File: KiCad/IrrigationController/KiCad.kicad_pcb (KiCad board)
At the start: 2 copper layers, 121.5 x 115 mm, 118 parts, among them IC1 MCP23017-E_SO, IC2 MCP23017-E_SO, IC3 DS89C21TMX_NOPB, J1 Screw_Terminal_01x03, J10 Screw_Terminal_01x05, J11 Screw_Terminal_01x02, J12 Screw_Terminal_01x02, J13 Screw_Terminal_01x04, J14 Screw_Terminal_01x02, J15 Screw_Terminal_01x02, J16 Screw_Terminal_01x02, J17 Screw_Terminal_01x02, J18 Screw_Terminal_01x02, J19 Screw_Terminal_01x02, J2 Screw_Terminal_01x03, J21 Screw_Terminal_01x06, J3 Screw_Terminal_01x03, J5 Screw_Terminal_01x03, J6 Screw_Terminal_01x02, J7 Screw_Terminal_01x02, J8 Screw_Terminal_01x02, J9 Screw_Terminal_01x02, K1 2071556-9, K2 2071556-9, Q1 MMBT3906, Q11 MMBT3904, Q12 MMBT3904, Q2 MMBT3906, Q3 MMBT3906, Q6 MMBT3904, Q7 MMBT3904, Q8 MMBT3904, SW1 SW_Push, U1 L298P, U2 ARDUINO_MKR_WAN_1310, U3 L298P, U4 L298P, U5 L298P, U7 L7805

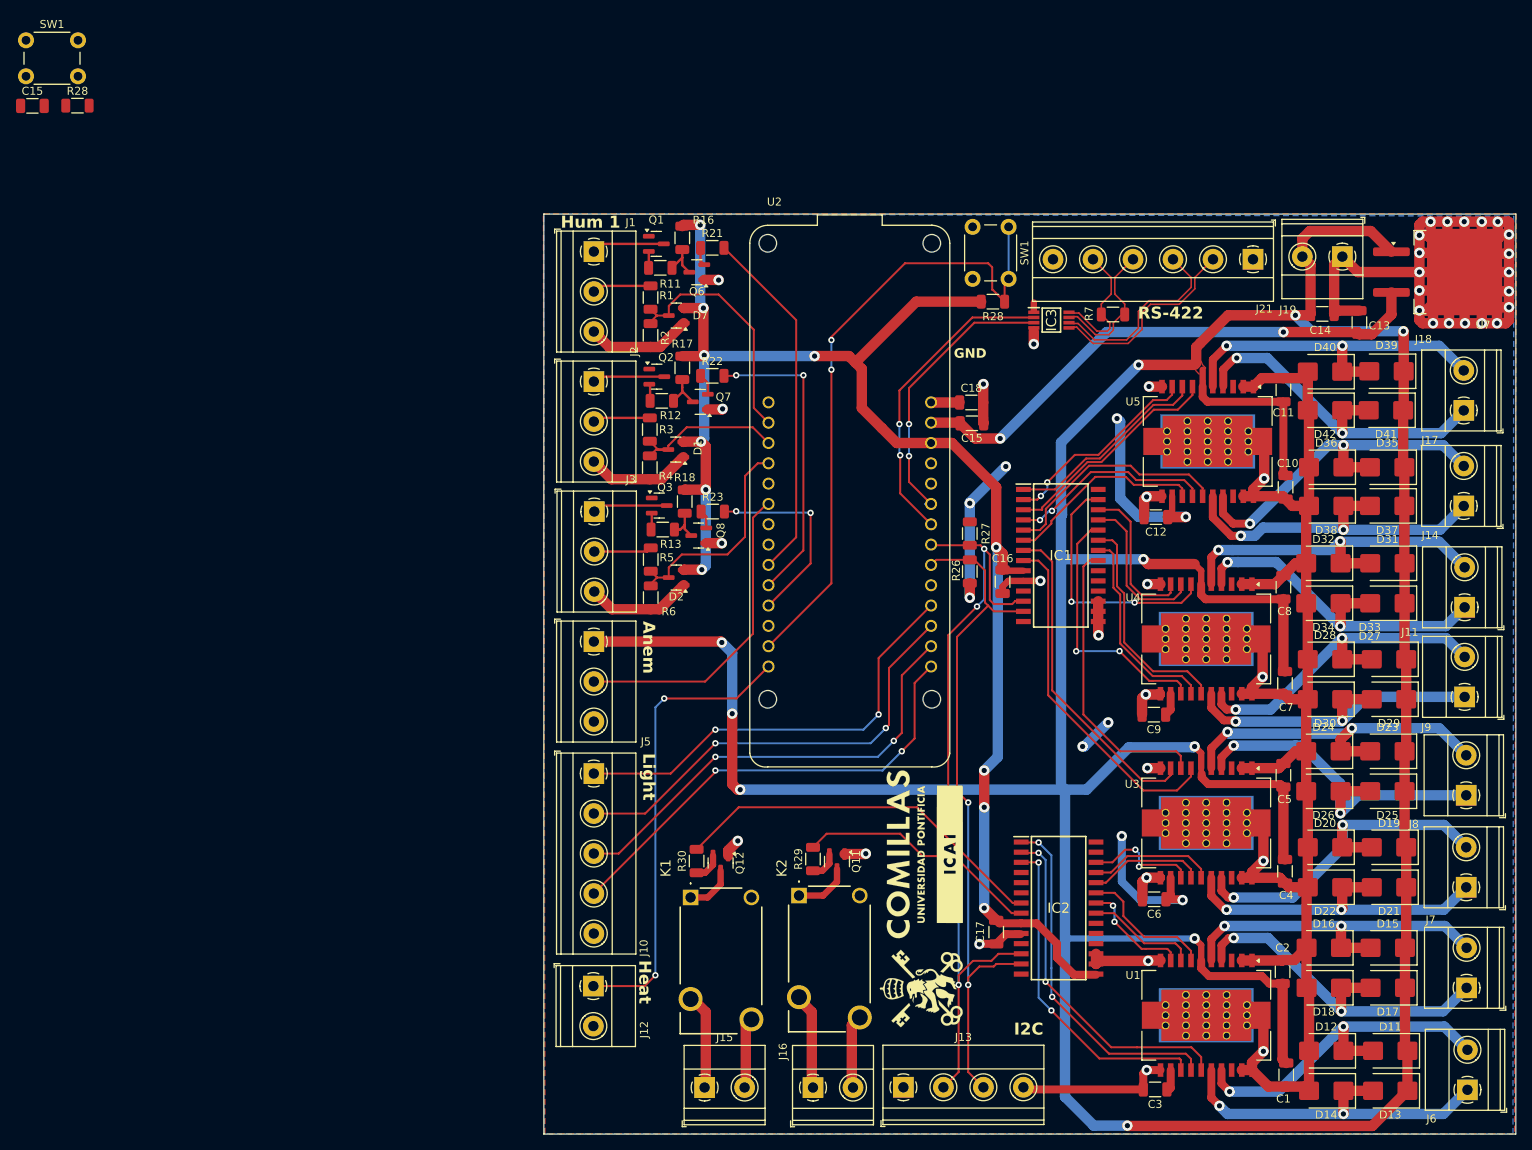
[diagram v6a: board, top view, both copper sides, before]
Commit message: Fixed remaining mistakes | wrong transistor + rs422 footprints
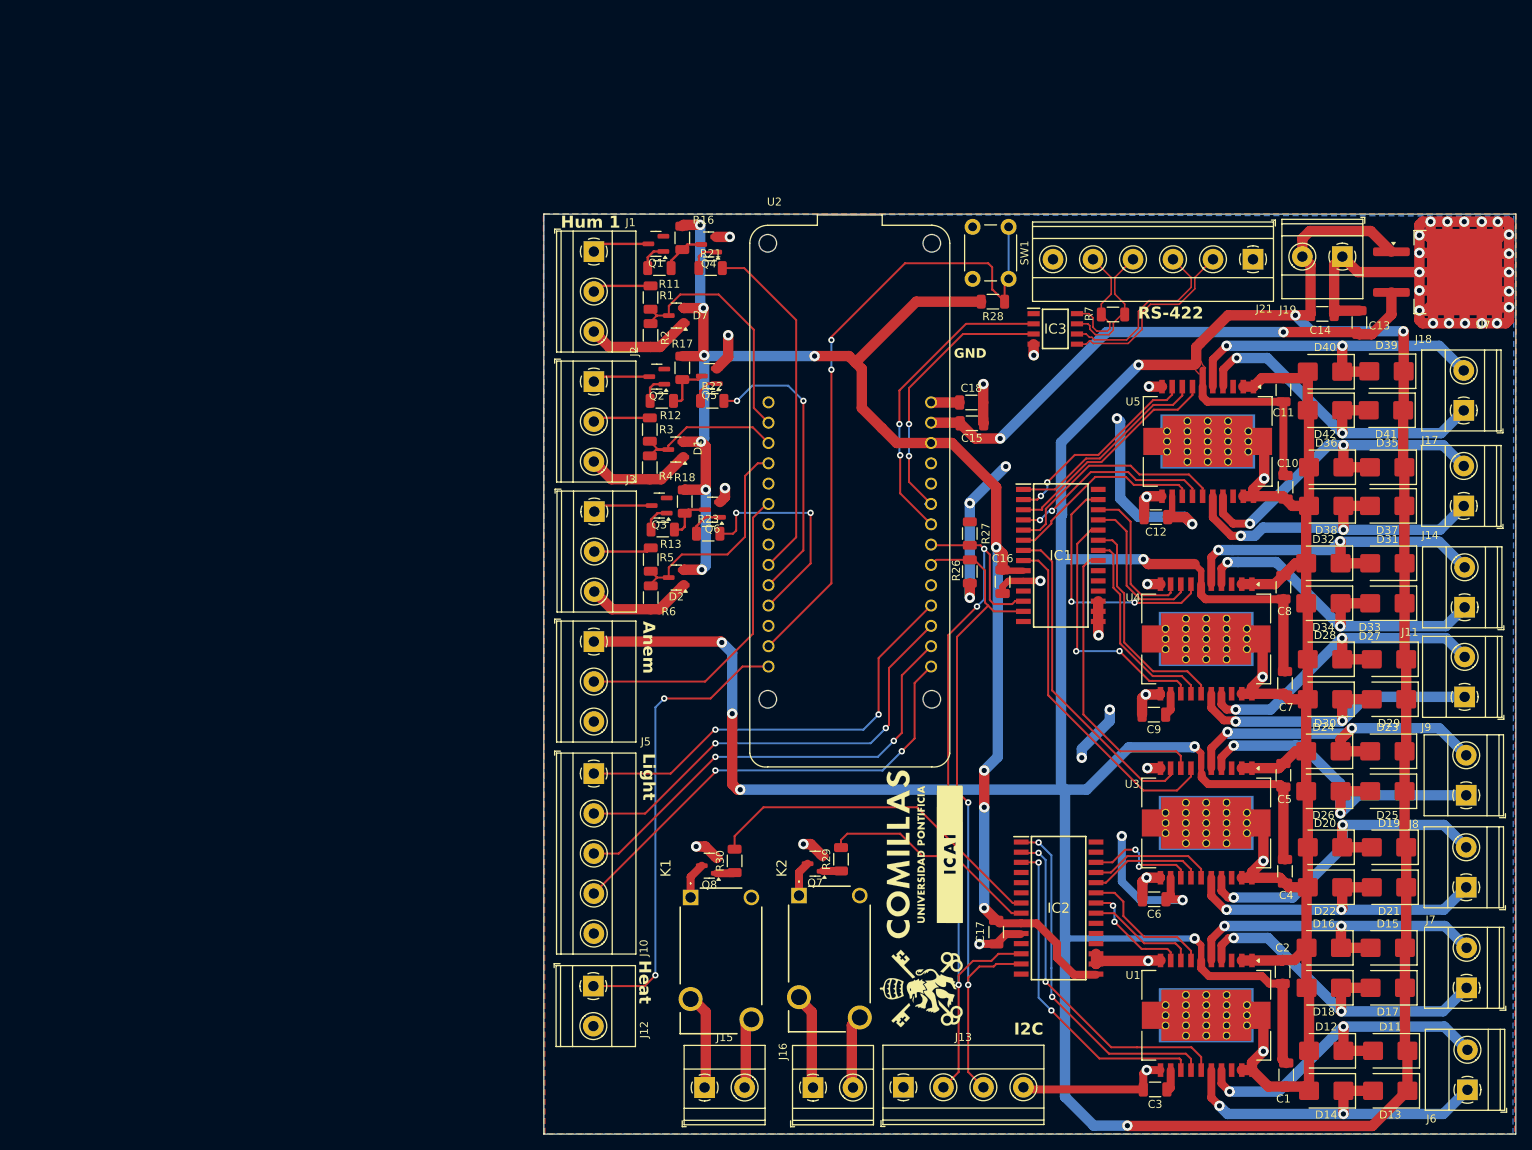
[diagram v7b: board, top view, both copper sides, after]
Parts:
- removed the C15 at (2.33, 9.72)
- removed Q11, Q12: MMBT3904, Package_TO_SOT_SMD:SOT-23
- removed the R28 at (7.96, 9.70)
- removed the SW1 at (1.52, 1.52)
- added Q4: MMBT3904, Package_TO_SOT_SMD:SOT-23, F.Cu at (86.9, 27.1)
- added Q5: MMBT3904, Package_TO_SOT_SMD:SOT-23, F.Cu at (86.9, 43.5)
- IC3: footprint SamacSys_Parts:SOP65P490X110-8N -> SamacSys_Parts:SOIC127P600X175-8N
- moved Q7 59.5 mm to (100.2, 104.5)
- moved Q8 41.3 mm to (86.9, 104.7)
- moved Q6 29.7 mm to (87.3, 60.2)
- moved R30 4.75 mm to (90.1, 104.1)
- moved R29 3.50 mm to (103.4, 103.9)
- moved R22 3.13 mm to (87.3, 46.6)
- moved R23 2.82 mm to (86.8, 63.2)
- moved R21 2.54 mm to (87.1, 30.0)
- moved IC3 1.21 mm to (130.2, 37.6)
- moved R11 0.12 mm to (80.7, 30.0)
- turned Q1 to 180 degrees
- turned Q2 to 180 degrees
- turned Q3 to 180 degrees
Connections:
- Q1 pad 1: +5V -> Net-(Q1-B)
- Q1 pad 2: Net-(Q1-B) -> +5V
- Q2 pad 1: +5V -> Net-(Q2-B)
- Q2 pad 2: Net-(Q2-B) -> +5V
- Q3 pad 1: +5V -> Net-(Q3-B)
- Q3 pad 2: Net-(Q3-B) -> +5V
- Q6 pad 1: Earth -> Net-(Q6-B)
- Q6 pad 2: Net-(Q6-B) -> Earth
- Q7 pad 1: Earth -> Net-(Q7-B)
- Q7 pad 2: Net-(Q7-B) -> Earth
- Q7 pad 3: Net-(Q7-C) -> Net-(K2-COIL_1)
- Q8 pad 1: Earth -> Net-(Q8-B)
- Q8 pad 2: Net-(Q8-B) -> Earth
- Q8 pad 3: Net-(Q8-C) -> Net-(K1-COIL_1)
- R11 pad 1: Net-(Q6-C) -> Net-(Q4-C)
- R12 pad 1: Net-(Q7-C) -> Net-(Q5-C)
- R13 pad 1: Net-(Q8-C) -> Net-(Q6-C)
- R16 pad 1: Net-(Q6-C) -> Net-(Q4-C)
- R17 pad 1: Net-(Q7-C) -> Net-(Q5-C)
- R18 pad 1: Net-(Q8-C) -> Net-(Q6-C)
- R21 pad 1: Net-(Q6-B) -> Net-(Q4-B)
- R22 pad 1: Net-(Q7-B) -> Net-(Q5-B)
- R23 pad 1: Net-(Q8-B) -> Net-(Q6-B)
- R29 pad 1: Net-(Q11-B) -> Net-(Q7-B)
- R30 pad 1: Net-(Q12-B) -> Net-(Q8-B)
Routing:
- net Net-(Q5-C): track 0.00 -> 6.29 mm
- net Net-(Q4-C): track 0.00 -> 5.52 mm
- net Net-(Q7-C): track 4.98 -> 0.00 mm
- net Net-(Q8-C): track 4.64 -> 0.00 mm
- net +5V: track 78.5 -> 82.8 mm
- net Net-(Q4-B): track 0.00 -> 3.83 mm
- net Earth: track 523.3 -> 527.1 mm
- net /RELAY_1_EN: track 47.7 -> 43.9 mm
- net Net-(Q5-B): track 0.00 -> 3.65 mm
- net Net-(Q12-B): track 3.62 -> 0.00 mm
- net Net-(Q11-B): track 3.62 -> 0.00 mm
- net /RELAY_2_EN: track 30.8 -> 27.9 mm
- net /S_HUM_3_EN: track 24.6 -> 27.5 mm
- net Net-(K2-COIL_1): track 7.05 -> 4.43 mm
- net Net-(Q6-B): track 2.29 -> 4.34 mm
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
